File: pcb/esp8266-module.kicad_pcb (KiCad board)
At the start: 2 copper layers, 37.4 x 38.3 mm, 15 parts, among them U1 ESP-12E

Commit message: re-map I/O
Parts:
- added C-SWITCH1: C, Capacitor_SMD:C_0805_2012Metric, F.Cu at (38.8, 53.4)
- added R-SWITCH1: 10K, Resistor_SMD:R_0805_2012Metric, F.Cu at (44.6, 58.6)
- added SW-SWITCH1: SW_Push, Button_Switch_SMD:SW_SPST_B3U-1000P-B, F.Cu at (41.4, 53.1)
- moved C-PIR1 25.9 mm to (61.6, 70.8), turned to 270 degrees
- moved R-PIR1 23.1 mm to (44.6, 64.9), turned to 0 degrees
- moved J-PIR1 21.3 mm to (56.5, 66.3), turned to 0 degrees
- moved C-MAGNET1 20.6 mm to (40.1, 66.2), turned to 180 degrees
- moved C-BOOT1 20.3 mm to (67.3, 57.4), turned to 0 degrees
- moved SW-BOOT1 17.4 mm to (68.0, 53.9)
- moved R-MAGNET1 17.2 mm to (44.6, 61.6), turned to 180 degrees
- moved R-BOOT3 17.0 mm to (66.4, 64.5)
- moved J-MAGNET1 16.9 mm to (35.9, 61.0)
- moved R-BOOT1 16.8 mm to (67.3, 59.5)
- moved R-BOOT2 16.7 mm to (67.2, 61.6)
- moved U1 16.4 mm to (49.0, 51.6)
- moved R-BOOT5 16.3 mm to (44.8, 55.5)
- moved R-BOOT4 16.3 mm to (44.8, 51.5)
- moved J-UART1 16.2 mm to (55.4, 34.8)
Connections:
- U1 pad 5: Net-(U1-Pad5) -> /GPIO_14
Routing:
- net VDD: track 78.0 -> 204.7 mm, vias 2 -> 8
- net GND: track 149.9 -> 112.0 mm
- net /GPIO_13: track 44.3 -> 26.6 mm, vias 2 -> 0
- net /GPIO_14: track 0.00 -> 13.8 mm
- net /GPIO_0: track 11.9 -> 8.95 mm
- net /GPIO_12: track 10.5 -> 12.1 mm
- net /RX: track 18.3 -> 17.4 mm
- net /nRST: track 13.1 -> 12.3 mm
- net Net-(R-BOOT3-Pad2): track 3.99 -> 3.42 mm
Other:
- board size 37.4 x 38.3 mm -> 36.5 x 39.9 mm

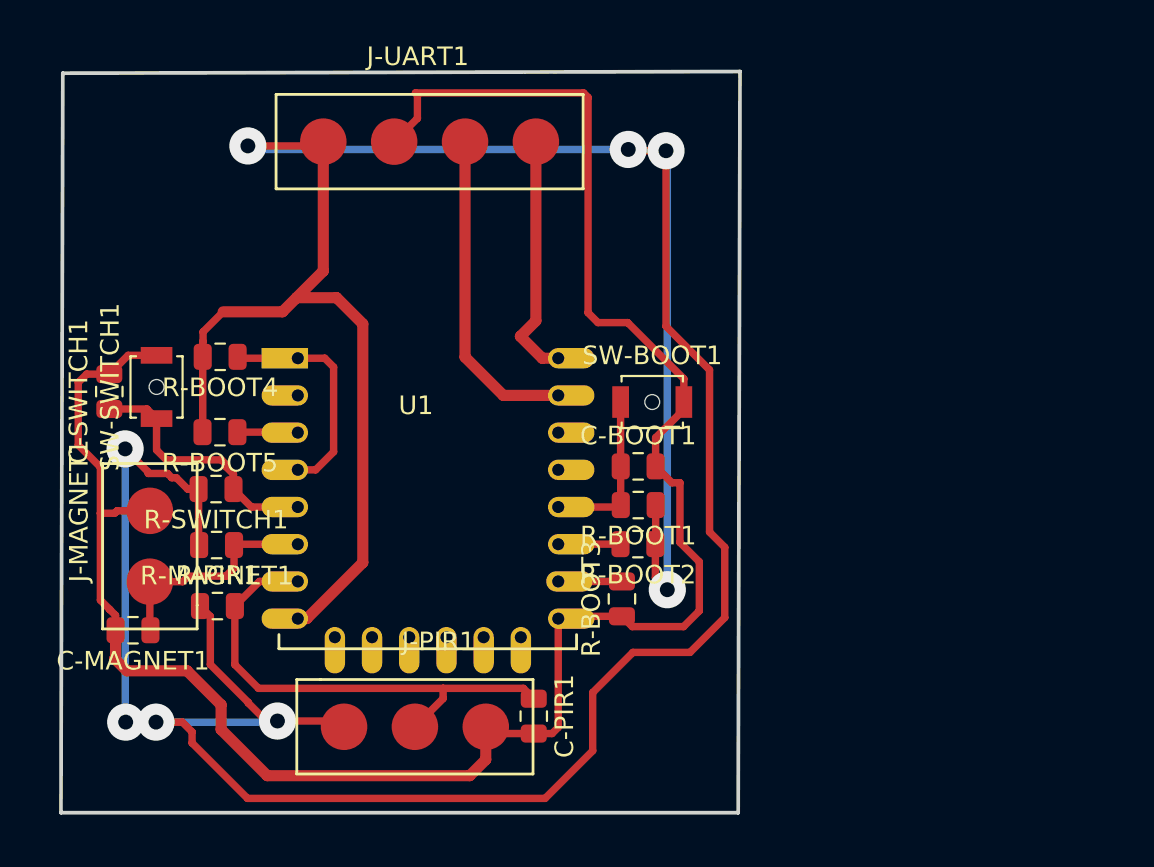
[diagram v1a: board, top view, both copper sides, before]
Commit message: Completing Transfer Copyright
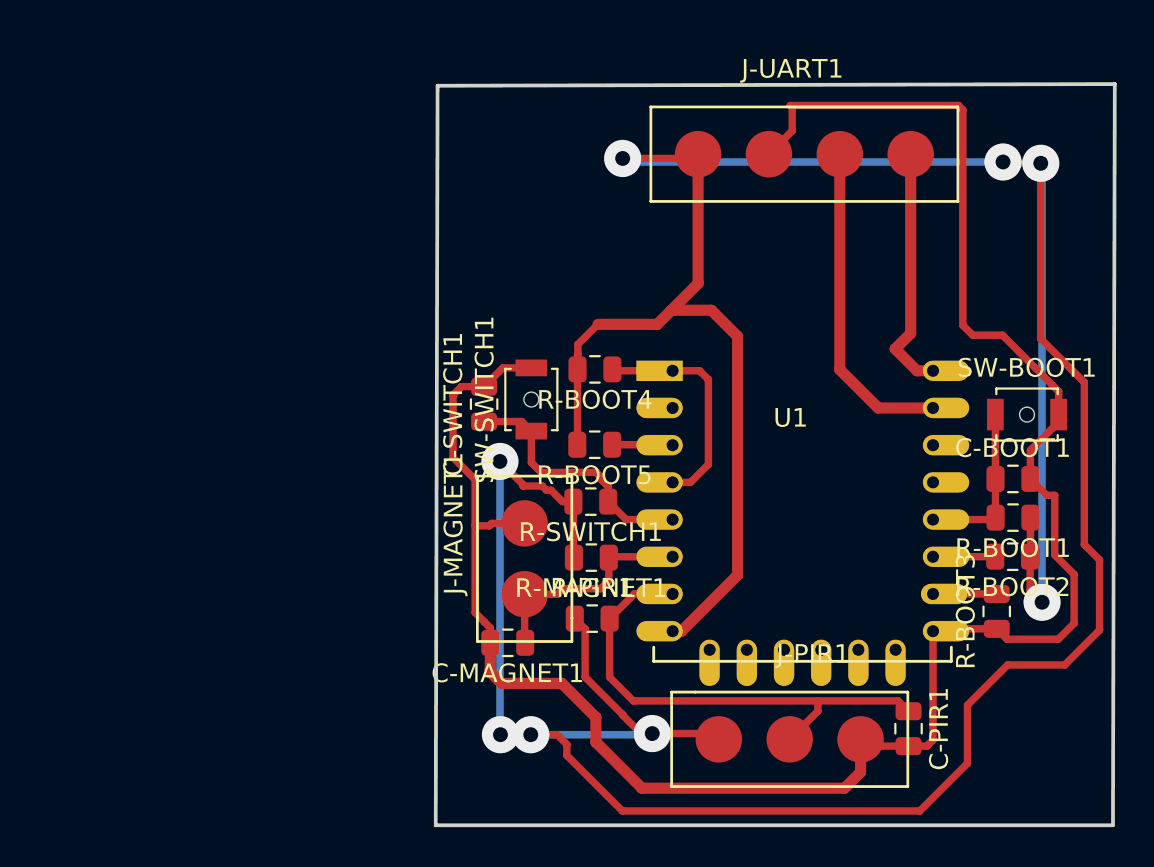
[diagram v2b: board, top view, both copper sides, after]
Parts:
- moved R-BOOT5 20.2 mm to (64.9, 56.2)
- moved U1 20.2 mm to (69.1, 52.2)
- moved C-BOOT1 20.2 mm to (87.4, 58.1)
- moved C-PIR1 20.2 mm to (81.8, 71.5)
- moved J-UART1 20.2 mm to (75.6, 35.5)
- moved R-BOOT1 20.2 mm to (87.4, 60.1)
- moved R-BOOT2 20.2 mm to (87.4, 62.2)
- moved R-BOOT3 20.2 mm to (86.5, 65.2)
- moved R-BOOT4 20.2 mm to (64.9, 52.2)
- moved J-MAGNET1 20.2 mm to (56.1, 61.7)
- moved C-MAGNET1 20.2 mm to (60.2, 66.9)
- moved C-SWITCH1 20.2 mm to (59.0, 54.0)
- moved J-PIR1 20.2 mm to (76.7, 67.0)
- moved R-MAGNET1 20.2 mm to (64.7, 62.3)
- moved R-PIR1 20.2 mm to (64.8, 65.6)
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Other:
- board size 36.5 x 39.9 mm -> 36.5 x 39.8 mm
